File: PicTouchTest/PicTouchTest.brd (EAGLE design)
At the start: 61.9 x 44.4 mm, 9 parts

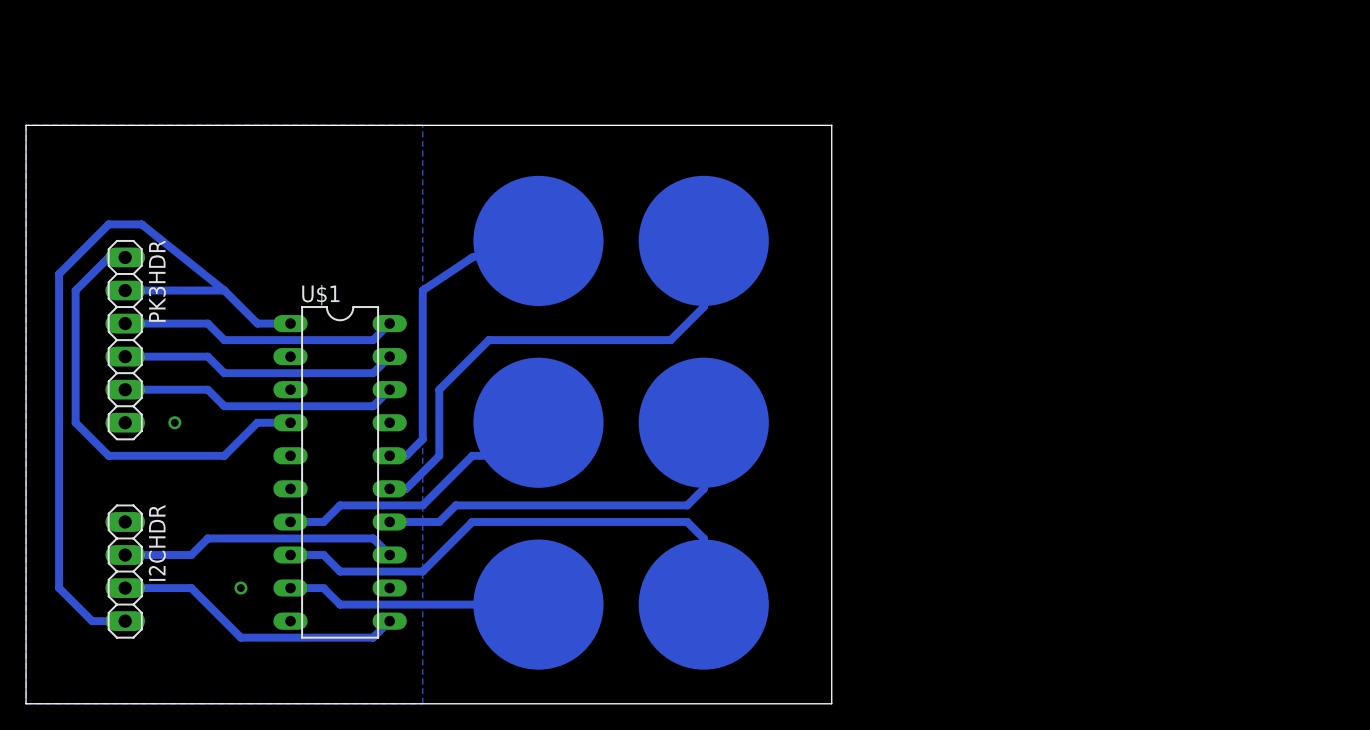
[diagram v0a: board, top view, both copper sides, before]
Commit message: Increase the touch button size to 20mm diameter.
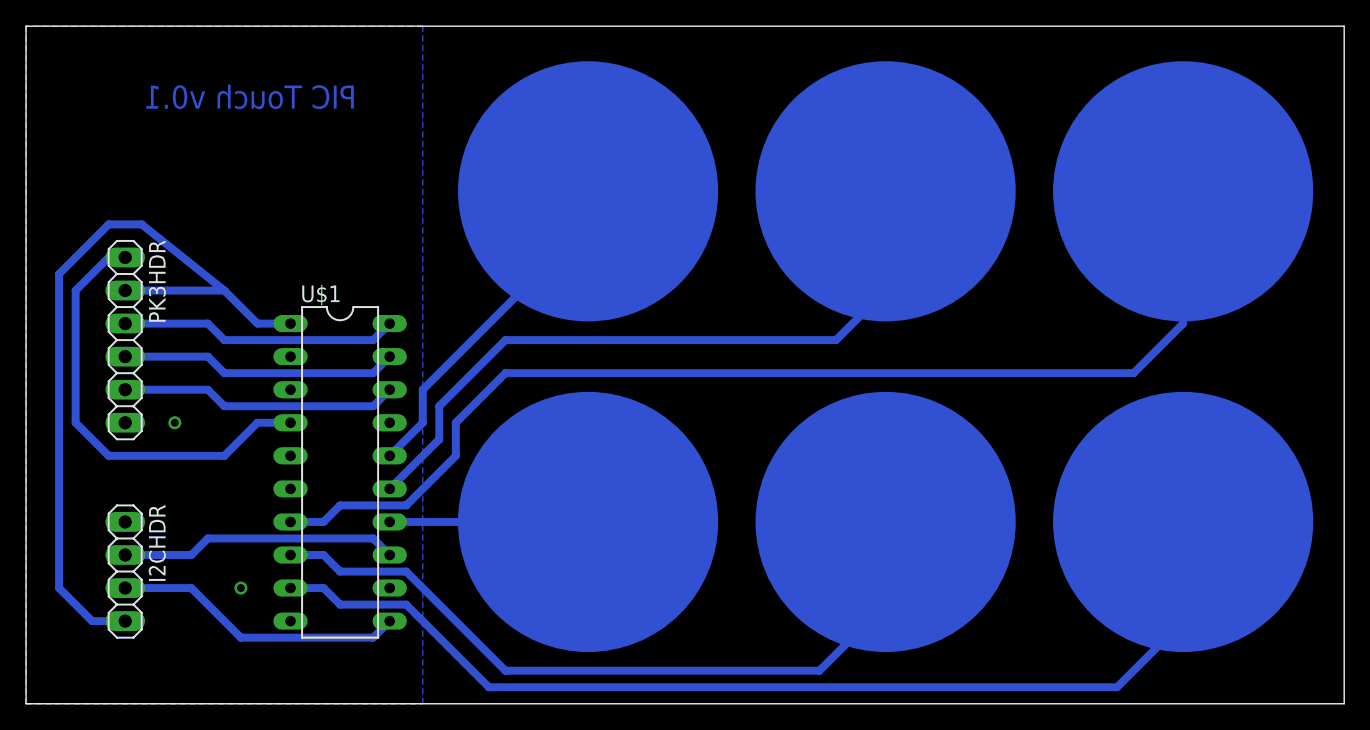
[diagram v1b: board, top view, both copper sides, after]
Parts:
- U$2, U$3, U$4, U$5, U$6, U$7: value CAPTOUCH -> CAPTOUCH20MMRND; device CapTouch:10MMROUND -> CapTouch:20MMROUND
- moved U$5 52.6 mm to (88.9, 39.4)
- moved U$7 49.9 mm to (88.9, 14.0)
- moved U$6 15.3 mm to (66.0, 14.0)
- moved U$3 14.5 mm to (66.0, 39.4)
- moved U$4 11.7 mm to (43.2, 14.0)
- moved U$2 5.39 mm to (43.2, 39.4)
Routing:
- net N$9: track 22.7 -> 86.5 mm
- net N$11: track 19.6 -> 81.5 mm
- net N$10: track 39.5 -> 57.9 mm
- net N$7: track 38.0 -> 53.5 mm
- net N$8: track 30.3 -> 15.2 mm
- net N$6: track 24.3 -> 26.6 mm
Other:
- board size 61.9 x 44.4 mm -> 101.3 x 52.1 mm
- board text added: "PIC Touch v0.1"
